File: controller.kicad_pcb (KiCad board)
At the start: 2 copper layers, 25 parts, among them J1 Conn_01x04, J2 Conn_01x08, J3 Conn_01x16, SW1 SW_Push, U1 PRTR5V0U2X, U2 AT90USB1286-AU, Y1 16MHz

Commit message: completion?! finished all circuitry
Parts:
- moved R4 20.9 mm to (124.1, 92.8)
- moved R3 20.9 mm to (124.1, 88.8)
- moved R1 17.9 mm to (129.0, 96.0)
- moved USB1 17.6 mm to (131.0, 111.3)
- moved U1 17.5 mm to (131.0, 90.1), turned to 270 degrees
- moved R2 16.3 mm to (132.9, 96.0)
- moved F1 12.7 mm to (137.3, 96.0)
- moved R5 6.55 mm to (84.5, 89.9)
- moved C2 5.02 mm to (72.3, 82.8)
- moved C6 5.01 mm to (63.5, 82.7)
- moved U2 4.42 mm to (68.6, 94.0)
- moved R9 3.54 mm to (147.6, 87.3)
- moved C7 3.31 mm to (56.3, 88.1)
- moved C4 3.28 mm to (63.7, 106.4)
- moved Y1 3.27 mm to (68.6, 106.4)
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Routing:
- net GND: track 0.00 -> 183.3 mm, vias 0 -> 6
- net +5V: track 0.00 -> 164.2 mm, vias 0 -> 4
- net Net-(J2-Pad1): track 0.00 -> 89.3 mm, vias 0 -> 1
- net Net-(R9-Pad1): track 0.00 -> 88.7 mm, vias 0 -> 2
- net Net-(R8-Pad2): track 0.00 -> 86.8 mm, vias 0 -> 2
- net Net-(J2-Pad2): track 0.00 -> 85.5 mm, vias 0 -> 1
- net Net-(R7-Pad2): track 0.00 -> 85.0 mm, vias 0 -> 2
- net Net-(J2-Pad3): track 0.00 -> 82.4 mm, vias 0 -> 1
- net Net-(J2-Pad4): track 0.00 -> 79.3 mm, vias 0 -> 1
- net Net-(J2-Pad5): track 0.00 -> 76.3 mm, vias 0 -> 1
- net Net-(J2-Pad6): track 0.00 -> 73.0 mm, vias 0 -> 1
- net Net-(R4-Pad2): track 0.00 -> 72.1 mm, vias 0 -> 2
- net Net-(R3-Pad1): track 0.00 -> 71.5 mm, vias 0 -> 2
- net Net-(J2-Pad7): track 0.00 -> 70.7 mm, vias 0 -> 1
- net Net-(J2-Pad8): track 0.00 -> 67.3 mm, vias 0 -> 1
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- added copper zone on F.Cu, net GND
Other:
- board text added: "USB C Model M"
- board text added: "by ashpil"

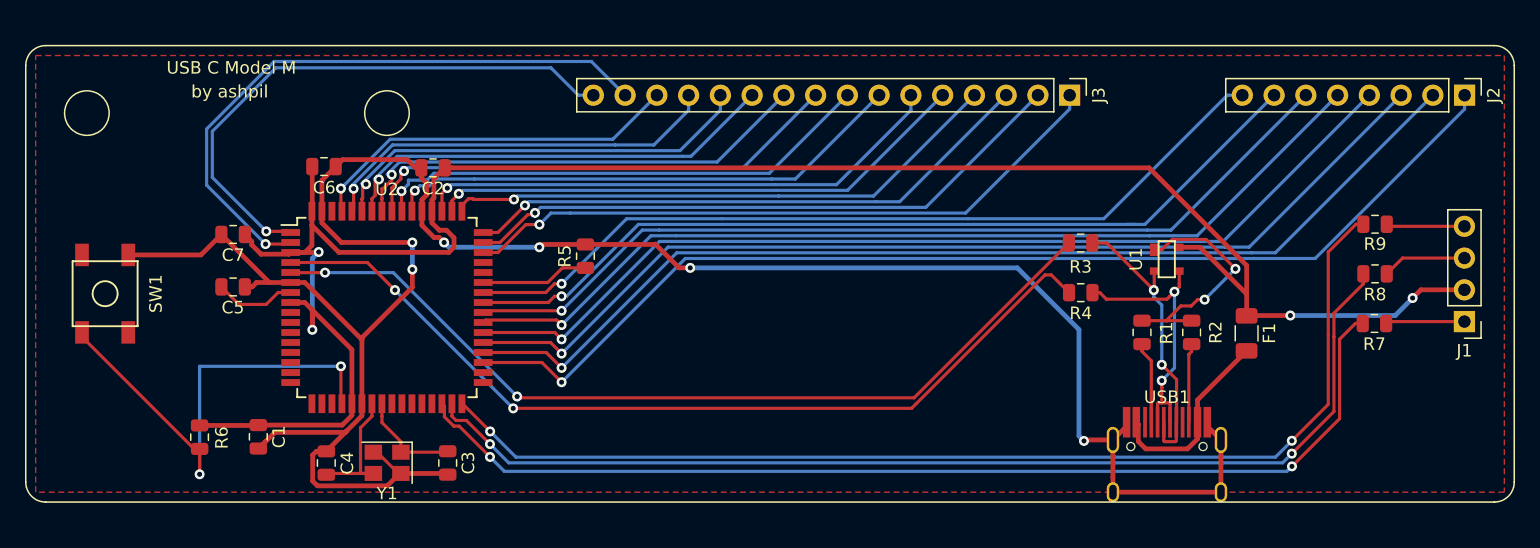
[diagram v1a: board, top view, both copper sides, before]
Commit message: misc tweaks for shield and usb pathing
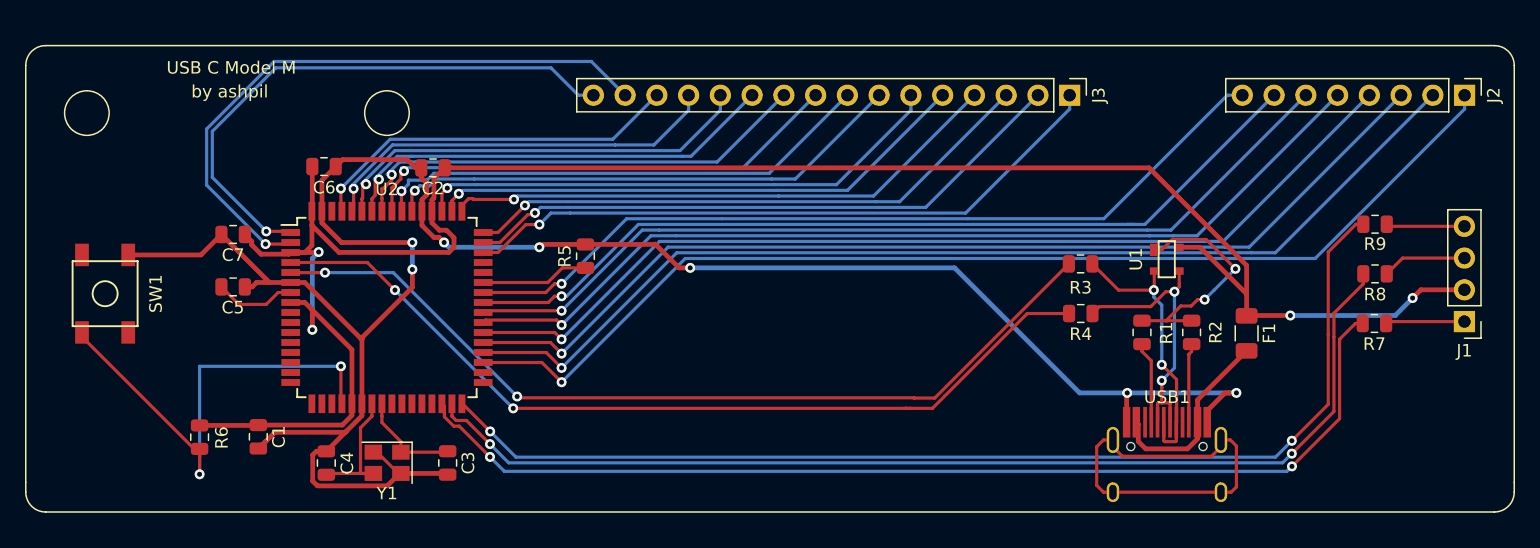
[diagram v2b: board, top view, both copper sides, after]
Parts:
- moved R3 1.67 mm to (124.1, 90.5)
- moved R4 1.67 mm to (124.1, 94.5)
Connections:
- USB1 pad 13: GND -> Net-(USB1-Pad13)
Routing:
- net Net-(USB1-Pad13): track 0.00 -> 31.3 mm
- net GND: track 183.3 -> 172.7 mm, vias 6 -> 7
- net Net-(R4-Pad2): track 72.1 -> 70.7 mm
- net D+: track 23.4 -> 22.7 mm
- net Net-(R3-Pad1): track 71.5 -> 70.9 mm
- removed copper zone on F.Cu, net GND

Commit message: clarified resistor value
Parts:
- R7, R8, R9: value 470 -> 470R
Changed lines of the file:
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@@
       (effects (font (size 1 1) (thickness 0.15)))
     )
-    (fp_text value 470 (at 0 -1.5875) (layer F.Fab)
+    (fp_text value 470R (at 0 -1.5875) (layer F.Fab)
       (effects (font (size 1 1) (thickness 0.15)))
     )
@@
       (effects (font (size 1 1) (thickness 0.15)))
     )
-    (fp_text value 470 (at 0 1.65) (layer F.Fab)
+    (fp_text value 470R (at 0 1.65) (layer F.Fab)
       (effects (font (size 1 1) (thickness 0.15)))
     )
@@
       (effects (font (size 1 1) (thickness 0.15)))
     )
-    (fp_text value 470 (at 0 1.65) (layer F.Fab)
+    (fp_text value 470R (at 0 1.65) (layer F.Fab)
       (effects (font (size 1 1) (thickness 0.15)))
     )

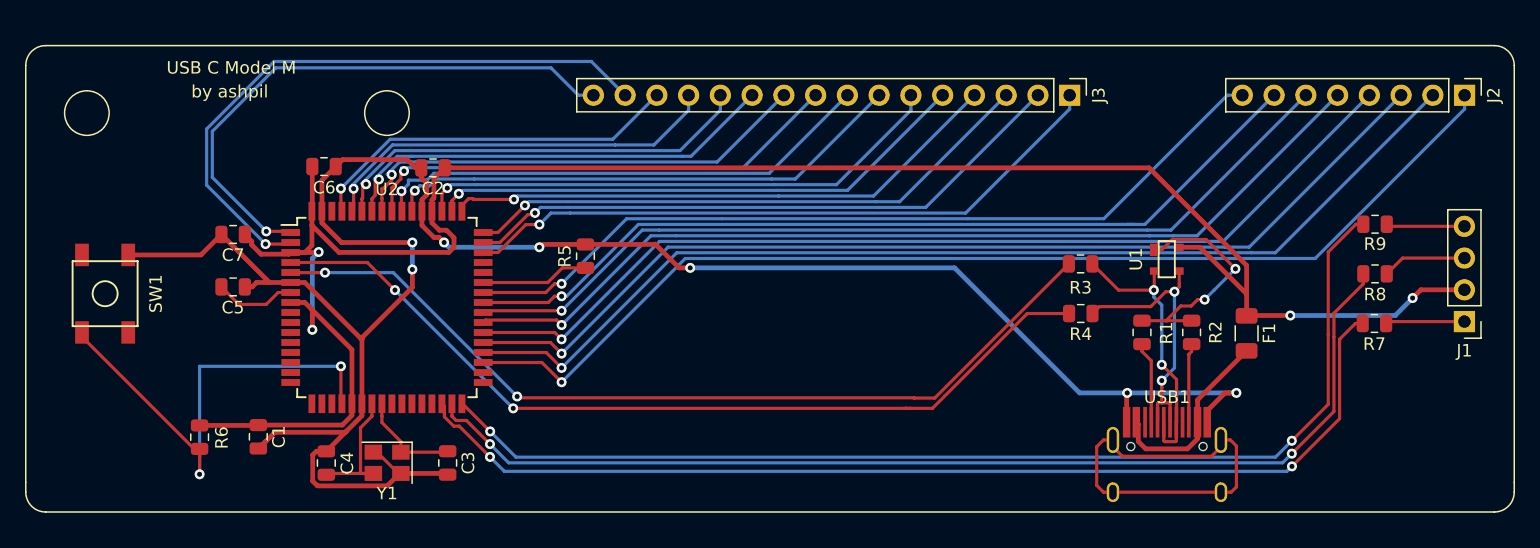
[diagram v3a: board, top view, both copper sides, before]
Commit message: made gound/5v/usb routing neater
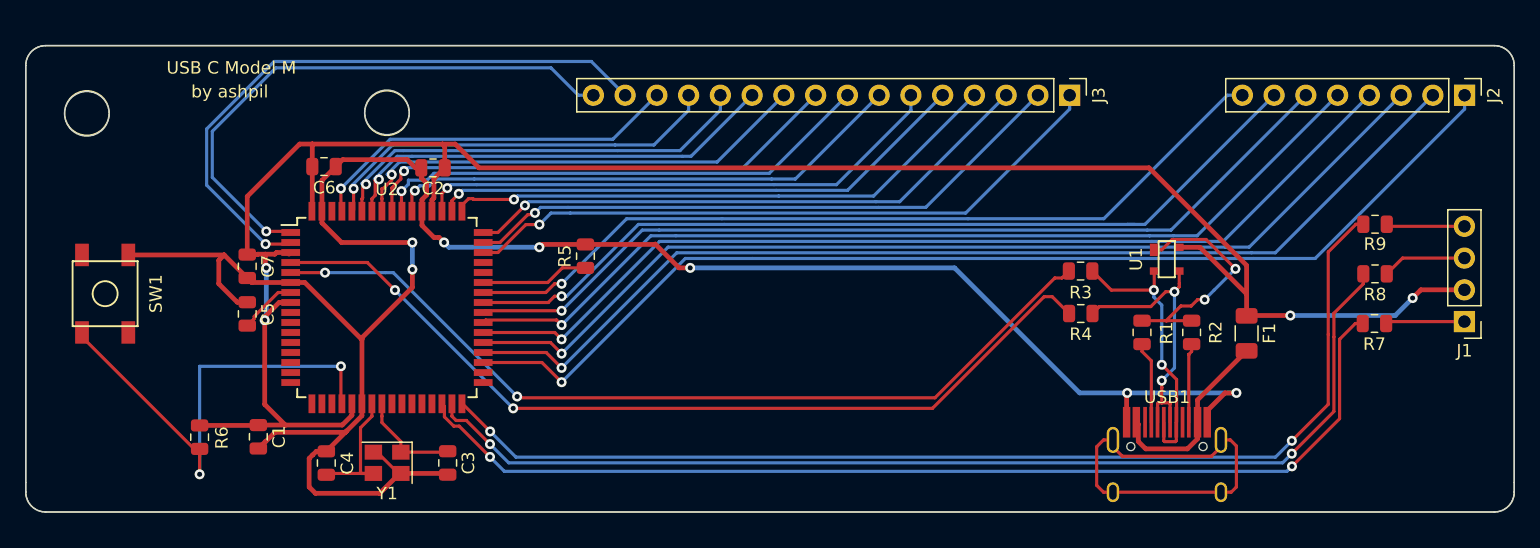
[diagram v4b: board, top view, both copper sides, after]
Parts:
- moved C7 2.78 mm to (57.4, 90.7), turned to 270 degrees
- moved C5 2.44 mm to (57.4, 94.5), turned to 90 degrees
- moved R3 0.57 mm to (124.1, 91.1)
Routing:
- net GND: track 172.7 -> 175.7 mm
- net Net-(C5-Pad1): track 6.51 -> 4.68 mm
- net +5V: track 164.2 -> 165.3 mm
- net Net-(R4-Pad2): track 70.7 -> 71.4 mm
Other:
- board outline added: 119.1 x 37.3 mm

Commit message: part list added
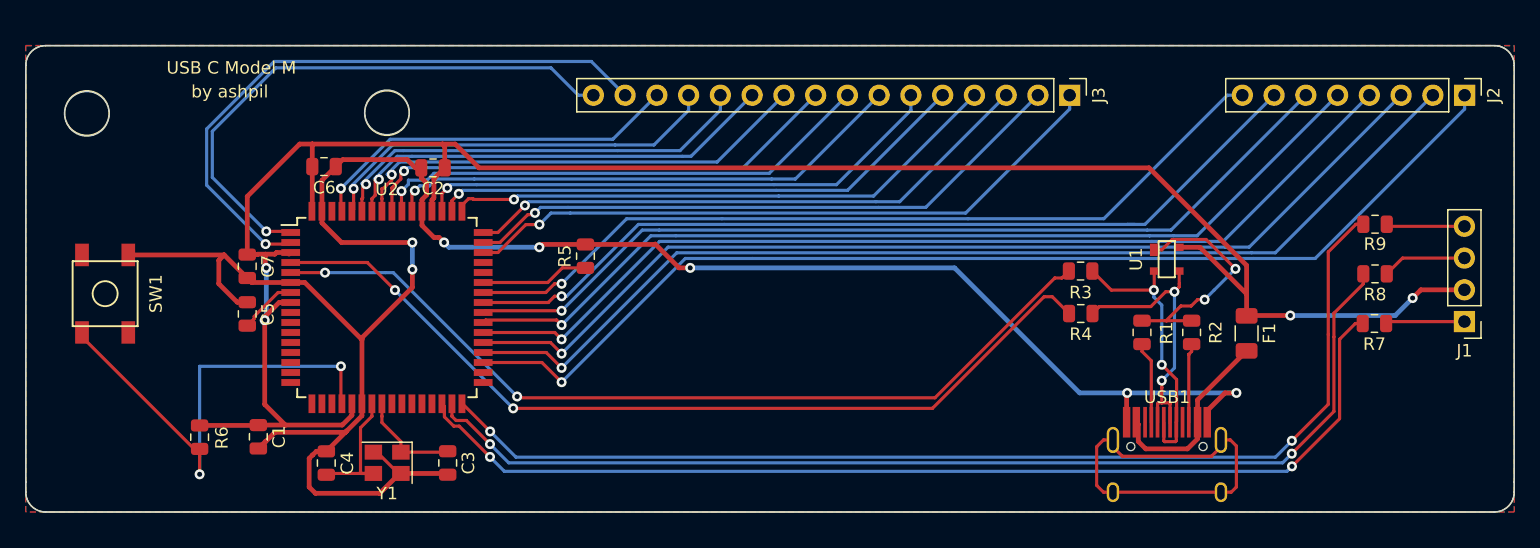
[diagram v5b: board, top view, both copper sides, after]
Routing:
- added copper zone on B.Cu, net GND
- added copper zone on F.Cu, net GND
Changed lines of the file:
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@@
     (37 F.SilkS user)
     (38 B.Mask user)
-    (39 F.Mask user)
+    (39 F.Mask user hide)
     (40 Dwgs.User user)
     (41 Cmts.User user)
@@
       (outputformat 1)
       (mirror false)
-      (drillshape 1)
+      (drillshape 0)
       (scaleselection 1)
-      (outputdirectory ""))
+      (outputdirectory "gerbers/"))
   )
   (net 0 "")
@@
   (segment (start 135.28875 104.56725) (end 136.04275 104.56725) (width 0.254) (layer F.Cu) (net 69))
   (segment (start 136.04275 104.56725) (end 136.525 105.0495) (width 0.254) (layer F.Cu) (net 69))
+  (zone (net 1) (net_name GND) (layer F.Cu) (hatch edge 0.508)
+    (connect_pads (clearance 0.508))
+    (min_thickness 0.254)
+    (fill yes (arc_segments 32) (thermal_gap 0.508) (thermal_bridge_width 0.508))
+    (polygon
+      (pts
+        (xy 39.6875 73.025) (xy 158.75 73.025) (xy 158.75 110.33125) (xy 39.6875 110.33125)
+      )
+    )
+  )
+  (zone (net 1) (net_name GND) (layer B.Cu) (hatch edge 0.508)
+    (connect_pads (clearance 0.508))
+    (min_thickness 0.254)
+    (fill yes (arc_segments 32) (thermal_gap 0.508) (thermal_bridge_width 0.508))
+    (polygon
+      (pts
+        (xy 39.6875 73.025) (xy 158.75 73.025) (xy 158.75 110.33125) (xy 39.6875 110.33125)
+      )
+    )
+  )
 )

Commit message: rev 2
Adjusted ucb-c location, fixed grounding error, changed some sizes to be more snug
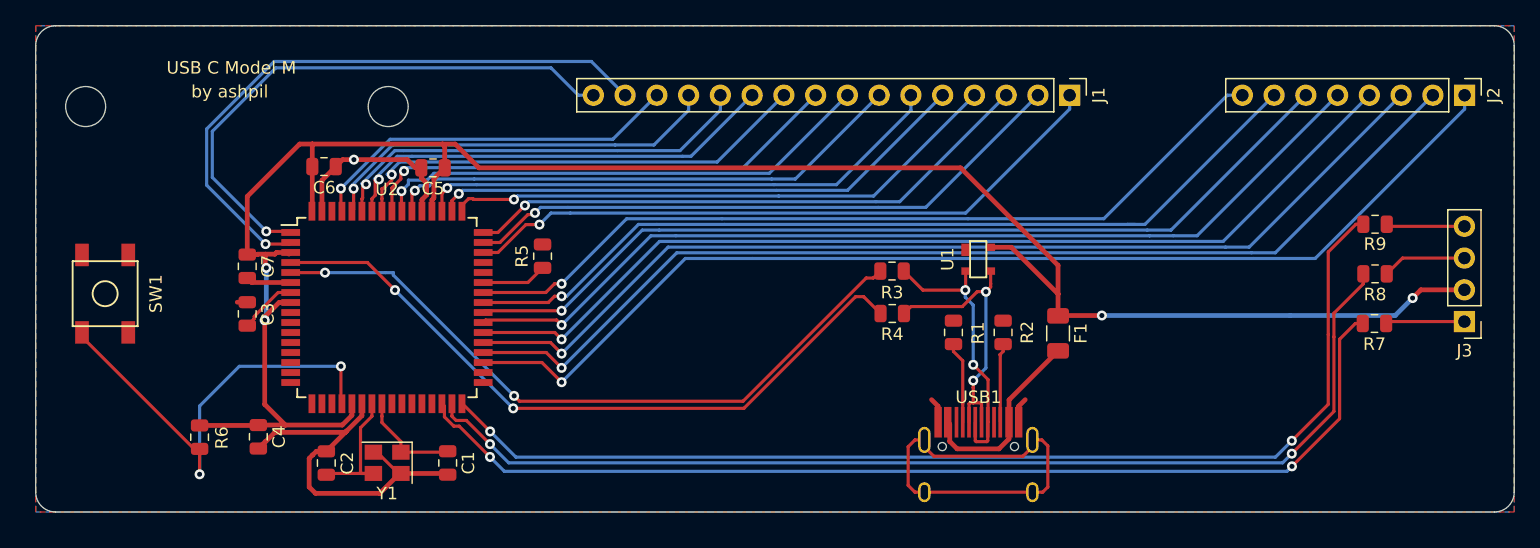
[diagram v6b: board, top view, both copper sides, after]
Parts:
- moved F1 15.1 mm to (122.3, 96.0)
- moved R1 15.1 mm to (113.9, 96.0)
- moved R2 15.1 mm to (117.9, 96.0)
- moved R3 15.1 mm to (109.0, 91.1)
- moved R4 15.1 mm to (109.0, 94.5)
- moved U1 15.1 mm to (115.9, 90.1)
- moved USB1 15.1 mm to (115.9, 111.3)
- moved R5 3.43 mm to (81.0, 89.9)
- renumbered C3 to C1, C4 to C2, C5 to C3, C1 to C4, C2 to C5, J3 to J1, J1 to J3
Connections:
- R1 pad 2: Net-(R1-Pad2) -> GND
- R2 pad 2: Net-(R1-Pad2) -> GND
- U1 pad 1: Net-(R1-Pad2) -> GND
- U2 pad 10: Net-(U2-Pad10) -> (no net)
- U2 pad 11: Net-(U2-Pad11) -> (no net)
- U2 pad 12: Net-(U2-Pad12) -> (no net)
- U2 pad 13: Net-(U2-Pad13) -> (no net)
- U2 pad 14: Net-(U2-Pad14) -> (no net)
- U2 pad 15: Net-(U2-Pad15) -> (no net)
- U2 pad 16: Net-(U2-Pad16) -> (no net)
- U2 pad 17: Net-(U2-Pad17) -> (no net)
- U2 pad 18: Net-(U2-Pad18) -> (no net)
- U2 pad 19: Net-(U2-Pad19) -> (no net)
- U2 pad 25: Net-(U2-Pad25) -> (no net)
- U2 pad 26: Net-(U2-Pad26) -> (no net)
- U2 pad 27: Net-(U2-Pad27) -> (no net)
- U2 pad 28: Net-(U2-Pad28) -> (no net)
- U2 pad 29: Net-(U2-Pad29) -> (no net)
- U2 pad 33: Net-(U2-Pad33) -> (no net)
- U2 pad 34: Net-(U2-Pad34) -> (no net)
- U2 pad 44: Net-(U2-Pad44) -> (no net)
- U2 pad 45: Net-(U2-Pad45) -> (no net)
- U2 pad 62: Net-(U2-Pad62) -> (no net)
- U2 pad 9: Net-(U2-Pad9) -> (no net)
- USB1 pad 3: Net-(USB1-Pad3) -> (no net)
- USB1 pad 9: Net-(USB1-Pad9) -> (no net)
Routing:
- net GND: track 175.7 -> 56.6 mm, vias 7 -> 1
- net Net-(R1-Pad2): track 19.2 -> 0.00 mm, vias 2 -> 0
- net Net-(R4-Pad2): track 71.4 -> 56.3 mm
- net Net-(R3-Pad1): track 70.6 -> 55.9 mm
- net Net-(R5-Pad1): track 8.66 -> 5.23 mm
- net Net-(R6-Pad2): track 39.1 -> 37.2 mm
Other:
- board size 119.1 x 37.3 mm -> 118.3 x 38.9 mm

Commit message: fixed LED connector
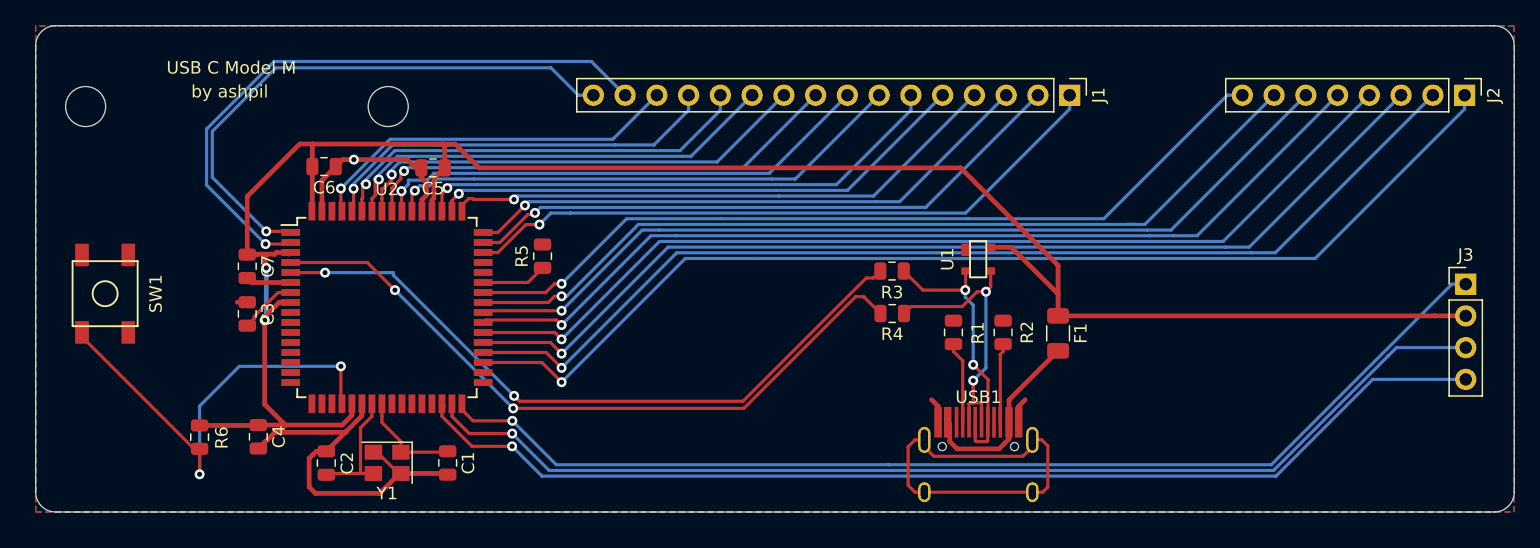
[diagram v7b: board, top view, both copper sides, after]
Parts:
- removed R7, R8, R9: 470R, Resistor_SMD:R_0805_2012Metric
- moved J3 3.00 mm to (154.9, 92.1), turned to 0 degrees
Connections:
- U2 pad 30: Net-(R7-Pad2) -> Net-(J3-Pad4)
- U2 pad 31: Net-(R8-Pad2) -> Net-(J3-Pad3)
- U2 pad 32: Net-(R9-Pad1) -> Net-(J3-Pad1)
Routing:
- net Net-(R9-Pad1): track 88.7 -> 0.00 mm, vias 2 -> 0
- net Net-(R8-Pad2): track 86.8 -> 0.00 mm, vias 2 -> 0
- net Net-(R7-Pad2): track 85.0 -> 0.00 mm, vias 2 -> 0
- net Net-(J3-Pad1): track 6.32 -> 88.6 mm, vias 0 -> 1
- net Net-(J3-Pad4): track 6.28 -> 88.4 mm, vias 0 -> 1
- net Net-(J3-Pad3): track 6.73 -> 88.0 mm, vias 0 -> 1
- net +5V: track 165.3 -> 164.6 mm, vias 4 -> 2
